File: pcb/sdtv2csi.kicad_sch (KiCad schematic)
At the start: 67 parts, among them J1 VIDEO_IN, J2 RPI_CSI_TOP, U1 ADV7280A-M, U2 NJM12888F18, Y1 ABM8G-28.63636MHZ

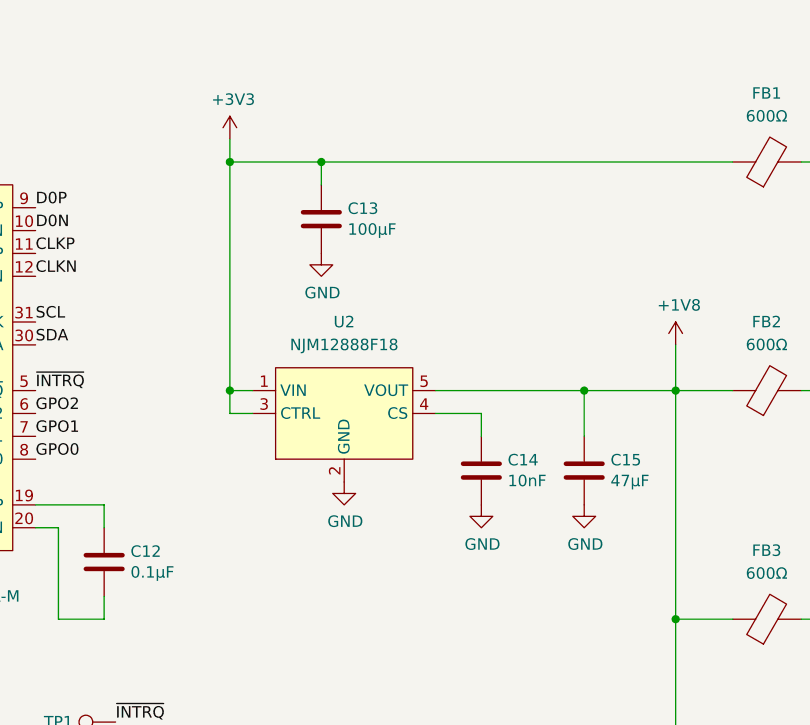
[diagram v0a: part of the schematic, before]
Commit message: Replacement of NJM12888F18 to TLV70218QDBVRQ1
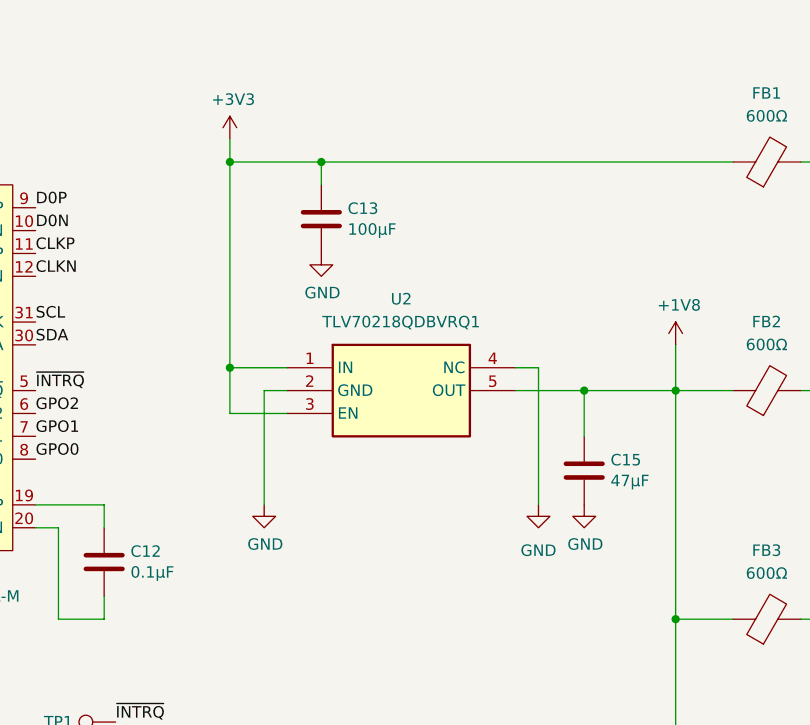
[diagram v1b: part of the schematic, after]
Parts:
- removed C14: 10nF, Capacitor_SMD:C_0402_1005Metric, symbol Device:C
- removed U2: NJM12888F18, Package_TO_SOT_SMD:SOT-23-5, symbol NJM12888F18:NJM12888F18
- added U2: TLV70218QDBVRQ1, SOT95P280X145-5N, symbol TLV70218QDBVRQ1:TLV70218QDBVRQ1
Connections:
- net +1V8: now also U2.5 (OUT)
- net +3V3: now also U2.1 (IN), U2.3 (EN)
- net GND: now also U2.2 (GND), U2.4 (NC)

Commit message: Update C9 / C10 and change ABM8G
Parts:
- C11, C9: value 20pF -> 10pF
- U2: footprint SOT95P280X145-5N -> Library:SOT95P280X145-5N
- Y1: value ABM8G-28.63636MHZ -> ABM8G-28.63636MHZ-4Y-T3
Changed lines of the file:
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@@
 			)
 		)
-		(property "Value" "ABM8G-28.63636MHZ"
+		(property "Value" "ABM8G-28.63636MHZ-4Y-T3"
 			(at 133.35 116.84 0)
 			(effects
@@
 			)
 		)
-		(property "Value" "20pF"
+		(property "Value" "10pF"
 			(at 117.221 123.063 0)
 			(effects
@@
 			)
 		)
-		(property "Value" "20pF"
+		(property "Value" "10pF"
 			(at 135.001 123.063 0)
 			(effects
@@
 			)
 		)
-		(property "Footprint" "SOT95P280X145-5N"
+		(property "Footprint" "Library:SOT95P280X145-5N"
 			(at 195.58 146.99 0)
 			(effects
